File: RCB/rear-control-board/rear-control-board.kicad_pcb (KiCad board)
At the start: 2 copper layers, 99.7 x 112.4 mm, 59 parts, among them J1 Conn_01x23, J2 Conn_01x23, J3 Conn_01x08, J4 JST-B2B-VERT-2PIN, J5 JST-B2B-VERT-2PIN, J6 FTSH-107-01-F-DV-K, K1 T9VV1K15-12S, K2 G5V-2, K3 G5V-2, U1 STM32F413CGUx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

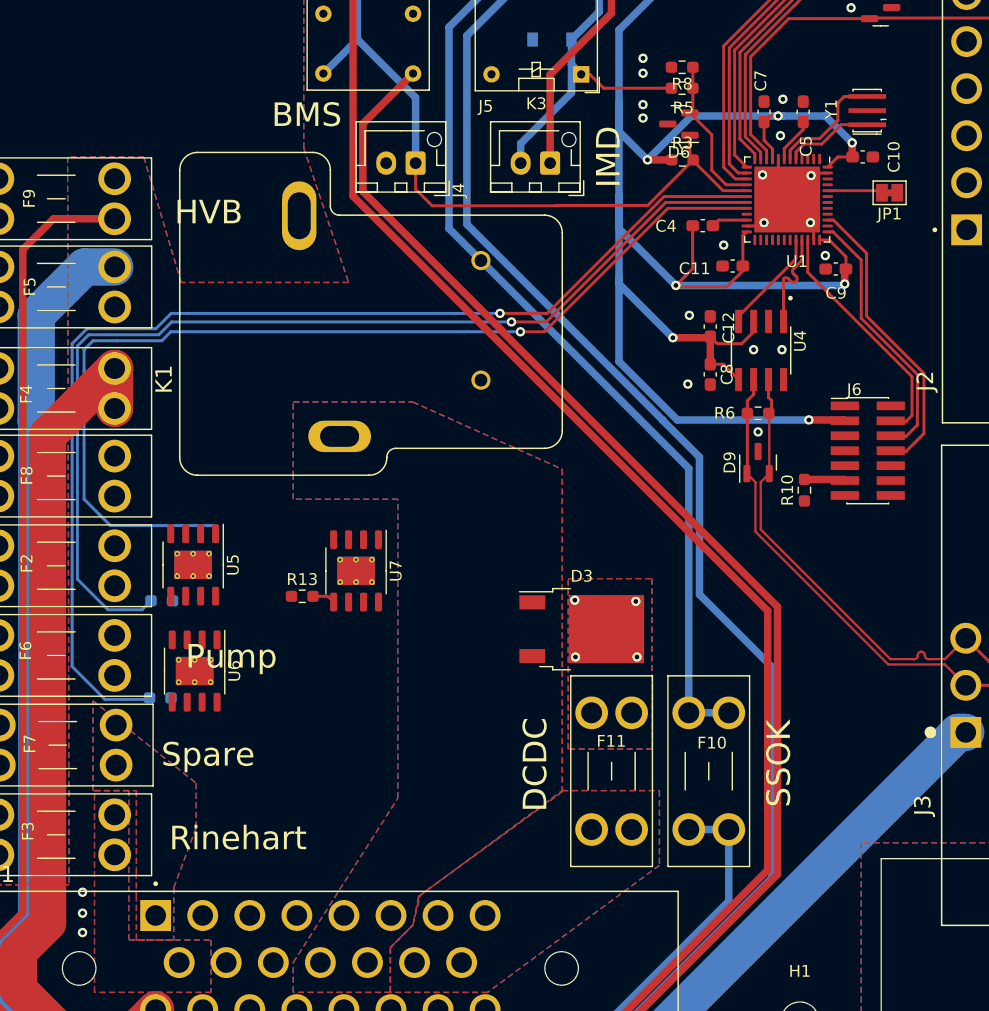
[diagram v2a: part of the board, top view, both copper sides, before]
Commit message: layout finished (need to place silkscreens)
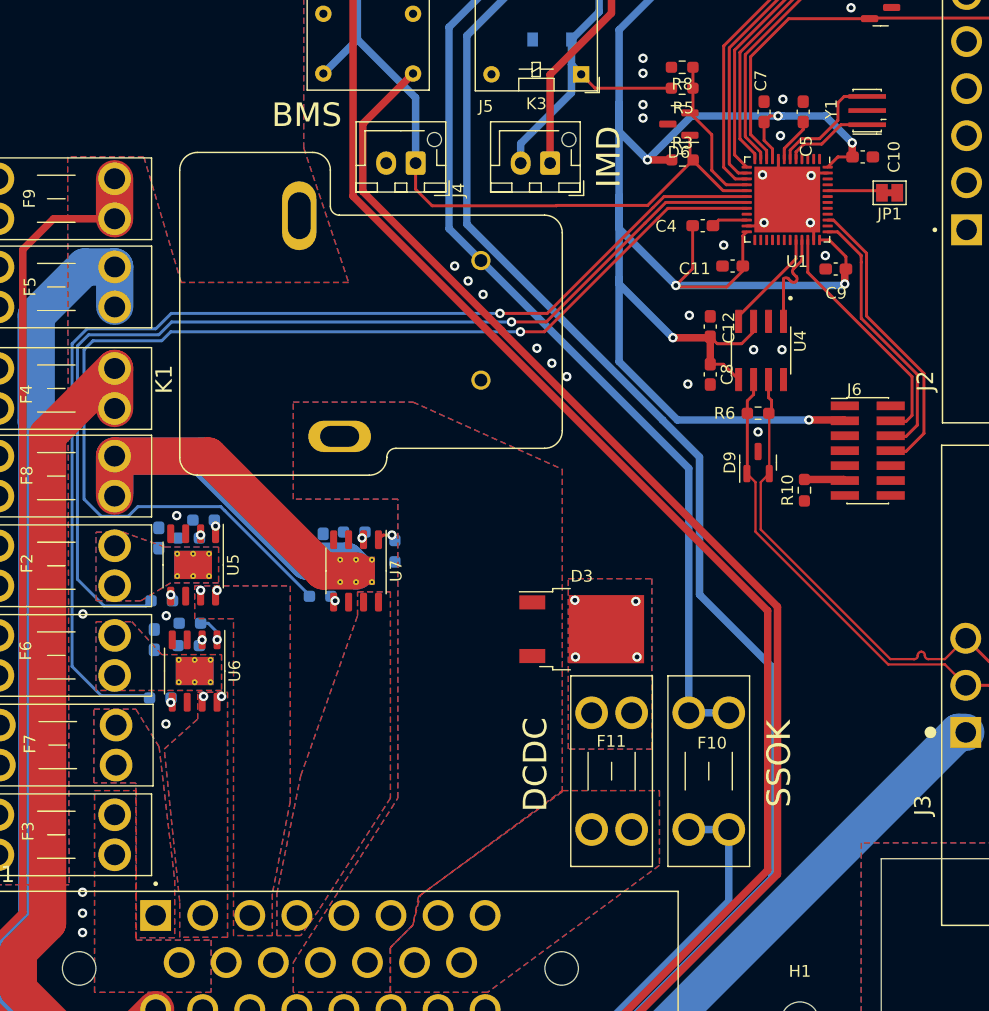
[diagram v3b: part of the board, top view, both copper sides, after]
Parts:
- added C13: 1u, Capacitor_SMD:C_0603_1608Metric_Pad1.08x0.95mm_HandSolder, B.Cu at (105.4, 120.7)
- added C2: 1u, Capacitor_SMD:C_0603_1608Metric_Pad1.08x0.95mm_HandSolder, B.Cu at (91.4, 120.1)
- added C3: 1u, Capacitor_SMD:C_0603_1608Metric_Pad1.08x0.95mm_HandSolder, B.Cu at (91.1, 128.8)
- added R1: 20k, Resistor_SMD:R_0603_1608Metric_Pad0.98x0.95mm_HandSolder, B.Cu at (95.2, 118.6)
- added R14: 20k, Resistor_SMD:R_0603_1608Metric_Pad0.98x0.95mm_HandSolder, B.Cu at (94.1, 127.4)
- added R15: 50k, Resistor_SMD:R_0603_1608Metric_Pad0.98x0.95mm_HandSolder, B.Cu at (94.0, 129.3)
- added R16: 20k, Resistor_SMD:R_0603_1608Metric_Pad0.98x0.95mm_HandSolder, B.Cu at (111.5, 121.3)
- added R17: 200k, Resistor_SMD:R_0603_1608Metric_Pad0.98x0.95mm_HandSolder, B.Cu at (108.1, 119.6)
- added R9: 50k, Resistor_SMD:R_0603_1608Metric_Pad0.98x0.95mm_HandSolder, B.Cu at (94.0, 120.1)
- R13: moved to B.Cu
- moved R13 1.52 mm to (105.2, 125.1)
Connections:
- U5 pad 1: unconnected-(U5-Pad1) -> Net-(U5-Pad1)
- U5 pad 2: unconnected-(U5-Pad2) -> Net-(U5-Pad2)
- U6 pad 1: unconnected-(U6-Pad1) -> Net-(U6-Pad1)
- U6 pad 2: unconnected-(U6-Pad2) -> Net-(U6-Pad2)
- U7 pad 1: unconnected-(U7-Pad1) -> Net-(U7-Pad1)
- U7 pad 2: unconnected-(U7-Pad2) -> Net-(U7-Pad2)
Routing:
- net /BRAKE_12V: track 0.00 -> 55.7 mm
- net /Controller/BRAKE_CTRL: track 86.1 -> 97.3 mm
- net /FuseBank/BRB_LOOP: track 96.4 -> 99.8 mm
- net /REAR_12V: track 162.3 -> 165.6 mm
- net Net-(U6-Pad1): track 0.00 -> 2.36 mm, vias 0 -> 1
- net Net-(U7-Pad1): track 0.00 -> 1.87 mm, vias 0 -> 1
- net Net-(R13-Pad2): track 1.96 -> 0.70 mm, vias 0 -> 1
- net Net-(U7-Pad2): track 0.00 -> 0.81 mm, vias 0 -> 1
- net B3_TRACESWO: track 26.0 -> 25.3 mm
- net Net-(U6-Pad2): track 0.00 -> 0.59 mm, vias 0 -> 1
- net Net-(U6-Pad5): track 0.00 -> 0.52 mm, vias 0 -> 1
- net GND: track 16.9 -> 17.0 mm, vias 23 -> 33
- net Net-(U5-Pad2): vias 0 -> 1
- net Net-(U5-Pad1): vias 0 -> 1
- net Net-(R11-Pad2): vias 0 -> 1
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- added copper zone on B.Cu, net /BRAKE_CTRL_12V
- added copper zone on F.Cu, net /BRAKE_CTRL_12V
- added copper zone on B.Cu, net /FAN_12V
- added copper zone on F.Cu, net /FAN_12V
- added copper zone on B.Cu, net /FAN_CTRL_12V
- added copper zone on F.Cu, net /FAN_CTRL_12V
- added copper zone on B.Cu, net /PUMP_12V
- added copper zone on F.Cu, net /PUMP_12V
- added copper zone on B.Cu, net /PUMP_CTRL_12V
- added copper zone on F.Cu, net /PUMP_CTRL_12V
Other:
- board text removed: "HVB"
- board text removed: "Pump"
- board text removed: "Rinehart"
- board text removed: "Spare"

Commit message: finished schem and layout. Ready for Review
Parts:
- added G***: LOGO, AERO_Footprints:AERO_Logo_10x4mm, F.Cu at (83.8, 84.1)
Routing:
- net /REAR_12V: track 165.6 -> 169.1 mm
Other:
- board size 99.7 x 112.4 mm -> 99.7 x 113 mm

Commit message: updating layout notes
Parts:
- moved C11 28.1 mm to (145.2, 69.3)
- moved C13 28.1 mm to (110.4, 93.0)
- moved H1 28.1 mm to (151.0, 133.5)
- moved J2 28.1 mm to (165.1, 66.3)
- moved K1 28.1 mm to (111.8, 74.4)
- moved U7 28.1 mm to (113.2, 95.2)
- moved C10 28.1 mm to (156.3, 60.1)
- moved D8 28.1 mm to (157.8, 47.4)
- moved JP1 28.1 mm to (158.6, 63.1)
- moved K2 28.1 mm to (110.5, 35.2)
- moved R4 28.1 mm to (155.9, 38.3)
- moved R5 28.1 mm to (140.9, 54.2)
- moved R7 28.1 mm to (161.2, 41.1)
- moved C1 28.1 mm to (140.4, 42.2)
- moved C12 28.1 mm to (143.3, 74.5)
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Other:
- board text removed: "bring decaps closer can pins on connect doens't need to be big use stm32 standard programming header, 5x10 1.27 pitch -> harwin (the one on the stlink mini) from stm32 go 2.54 then larger (15mil) add via near decoupling pins on caps use 8mil trace minimum check zone spacing, min is 8/8 (thickness/spacing) higher for 12V"

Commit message: touching up layout and making gerbers
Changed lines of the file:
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@@
       (outputformat 1)
       (mirror false)
-      (drillshape 1)
+      (drillshape 0)
       (scaleselection 1)
-      (outputdirectory "")
+      (outputdirectory "RCB_Gerber/")
     )
   )
@@
     (fp_line (start 0 -1.35) (end 0.625 -2.35) (layer "F.Fab") (width 0.1))
     (pad "" np_thru_hole circle locked (at -1.6 2 180) (size 1.2 1.2) (drill 1.2) (layers *.Cu *.Mask))
-    (pad "1" thru_hole roundrect locked (at 0 0 180) (size 1.7 2) (drill 1) (layers *.Cu *.Mask) (roundrect_rratio 0.147059)
+    (pad "1" thru_hole roundrect locked (at 0 0 180) (size 1.7 2) (drill 1) (layers *.Cu *.Mask) (roundrect_rratio 0.1470588235)
       (net 8 "/FAULT_LATCHER/BMS_SWITCH") (pinfunction "Pin_1") (pintype "passive"))
     (pad "2" thru_hole oval locked (at 2.5 0 180) (size 1.7 2) (drill 1) (layers *.Cu *.Mask)
@@
     (fp_line (start 3.5 -3.5) (end 3.5 3.5) (layer "F.Fab") (width 0.1))
     (fp_line (start 3.5 3.5) (end -3.5 3.5) (layer "F.Fab") (width 0.1))
-    (pad "" smd roundrect locked (at -2.1 0.7 270) (size 1.13 1.13) (layers "F.Paste") (roundrect_rratio 0.221239))
-    (pad "" smd roundrect locked (at -0.7 2.1 270) (size 1.13 1.13) (layers "F.Paste") (roundrect_rratio 0.221239))
-    (pad "" smd roundrect locked (at -0.7 -0.7 270) (size 1.13 1.13) (layers "F.Paste") (roundrect_rratio 0.221239))
-    (pad "" smd roundrect locked (at 0.7 2.1 270) (size 1.13 1.13) (layers "F.Paste") (roundrect_rratio 0.221239))
-    (pad "" smd roundrect locked (at 0.7 -0.7 270) (size 1.13 1.13) (layers "F.Paste") (roundrect_rratio 0.221239))
-    (pad "" smd roundrect locked (at -2.1 -2.1 270) (size 1.13 1.13) (layers "F.Paste") (roundrect_rratio 0.221239))
-    (pad "" smd roundrect locked (at 2.1 -0.7 270) (size 1.13 1.13) (layers "F.Paste") (roundrect_rratio 0.221239))
-    (pad "" smd roundrect locked (at 2.1 2.1 270) (size 1.13 1.13) (layers "F.Paste") (roundrect_rratio 0.221239))
-    (pad "" smd roundrect locked (at 0.7 -2.1 270) (size 1.13 1.13) (layers "F.Paste") (roundrect_rratio 0.221239))
-    (pad "" smd roundrect locked (at 0.7 0.7 270) (size 1.13 1.13) (layers "F.Paste") (roundrect_rratio 0.221239))
-    (pad "" smd roundrect locked (at -0.7 0.7 270) (size 1.13 1.13) (layers "F.Paste") (roundrect_rratio 0.221239))
-    (pad "" smd roundrect locked (at 2.1 0.7 270) (size 1.13 1.13) (layers "F.Paste") (roundrect_rratio 0.221239))
-    (pad "" smd roundrect locked (at -0.7 -2.1 270) (size 1.13 1.13) (layers "F.Paste") (roundrect_rratio 0.221239))
-    (pad "" smd roundrect locked (at 2.1 -2.1 270) (size 1.13 1.13) (layers "F.Paste") (roundrect_rratio 0.221239))
-    (pad "" smd roundrect locked (at -2.1 2.1 270) (size 1.13 1.13) (layers "F.Paste") (roundrect_rratio 0.221239))
-    (pad "" smd roundrect locked (at -2.1 -0.7 270) (size 1.13 1.13) (layers "F.Paste") (roundrect_rratio 0.221239))
+    (pad "" smd roundrect locked (at -2.1 0.7 270) (size 1.13 1.13) (layers "F.Paste") (roundrect_rratio 0.2212389381))
+    (pad "" smd roundrect locked (at -0.7 2.1 270) (size 1.13 1.13) (layers "F.Paste") (roundrect_rratio 0.2212389381))
+    (pad "" smd roundrect locked (at -0.7 -0.7 270) (size 1.13 1.13) (layers "F.Paste") (roundrect_rratio 0.2212389381))
+    (pad "" smd roundrect locked (at 0.7 2.1 270) (size 1.13 1.13) (layers "F.Paste") (roundrect_rratio 0.2212389381))
+    (pad "" smd roundrect locked (at 0.7 -0.7 270) (size 1.13 1.13) (layers "F.Paste") (roundrect_rratio 0.2212389381))
+    (pad "" smd roundrect locked (at -2.1 -2.1 270) (size 1.13 1.13) (layers "F.Paste") (roundrect_rratio 0.2212389381))
+    (pad "" smd roundrect locked (at 2.1 -0.7 270) (size 1.13 1.13) (layers "F.Paste") (roundrect_rratio 0.2212389381))
+    (pad "" smd roundrect locked (at 2.1 2.1 270) (size 1.13 1.13) (layers "F.Paste") (roundrect_rratio 0.2212389381))
+    (pad "" smd roundrect locked (at 0.7 -2.1 270) (size 1.13 1.13) (layers "F.Paste") (roundrect_rratio 0.2212389381))
+    (pad "" smd roundrect locked (at 0.7 0.7 270) (size 1.13 1.13) (layers "F.Paste") (roundrect_rratio 0.2212389381))
+    (pad "" smd roundrect locked (at -0.7 0.7 270) (size 1.13 1.13) (layers "F.Paste") (roundrect_rratio 0.2212389381))
+    (pad "" smd roundrect locked (at 2.1 0.7 270) (size 1.13 1.13) (layers "F.Paste") (roundrect_rratio 0.2212389381))
+    (pad "" smd roundrect locked (at -0.7 -2.1 270) (size 1.13 1.13) (layers "F.Paste") (roundrect_rratio 0.2212389381))
+    (pad "" smd roundrect locked (at 2.1 -2.1 270) (size 1.13 1.13) (layers "F.Paste") (roundrect_rratio 0.2212389381))
+    (pad "" smd roundrect locked (at -2.1 2.1 270) (size 1.13 1.13) (layers "F.Paste") (roundrect_rratio 0.2212389381))
+    (pad "" smd roundrect locked (at -2.1 -0.7 270) (size 1.13 1.13) (layers "F.Paste") (roundrect_rratio 0.2212389381))
     (pad "1" smd roundrect locked (at -3.4375 -2.75 270) (size 0.875 0.25) (layers "F.Cu" "F.Paste" "F.Mask") (roundrect_rratio 0.25)
       (net 61 "unconnected-(U1-Pad1)") (pinfunction "VBAT") (pintype "power_in"))
@@
     (fp_line (start -2.45 3.4) (end 4.95 3.4) (layer "F.Fab") (width 0.1))
     (pad "" np_thru_hole circle locked (at -1.6 2 180) (size 1.2 1.2) (drill 1.2) (layers *.Cu *.Mask))
-    (pad "1" thru_hole roundrect locked (at 0 0 180) (size 1.7 2) (drill 1) (layers *.Cu *.Mask) (roundrect_rratio 0.147059)
+    (pad "1" thru_hole roundrect locked (at 0 0 180) (size 1.7 2) (drill 1) (layers *.Cu *.Mask) (roundrect_rratio 0.1470588235)
       (net 3 "INT_12V") (pinfunction "Pin_1") (pintype "passive"))
     (pad "2" thru_hole oval locked (at 2.5 0 180) (size 1.7 2) (drill 1) (layers *.Cu *.Mask)
